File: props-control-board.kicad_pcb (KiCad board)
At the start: 2 copper layers, 109.2 x 35.6 mm, 64 parts, among them J1 Conn_01x04_Female, J10 Conn_01x02_Female, J11 Conn_01x02_Female, J12 Conn_01x02_Female, J13 Conn_01x02_Female, J2 Conn_01x03_Female, J3 Conn_01x03_Female, J4 Conn_01x03_Female, J5 Conn_01x06_Female, J6 Conn_01x05_Female, J7 Conn_01x04_Female, J8 Conn_01x02_Female, J9 Conn_01x02_Female, Q1 DMN24H3D5L, Q2 DMN24H3D5L, Q3 DMN24H3D5L, Q4 DMN24H3D5L, Q5 DMN24H3D5L, Q6 DMN24H3D5L, Q7 DMN24H3D5L, Q8 DMN24H3D5L, U1 AZ1117-3.3, U10 HCPL2631SD, U11 RFM-0505S, U2 VOS628A, U3 arduino_pro_mini, U4 STM32F042K6T6, U5 TXB0101DCKT, U6 TXB0104PWR, U7 AZ1117-3.3, U8 SX1278_module, U9 HCPL2631SD, Y1 Crystal_GND24

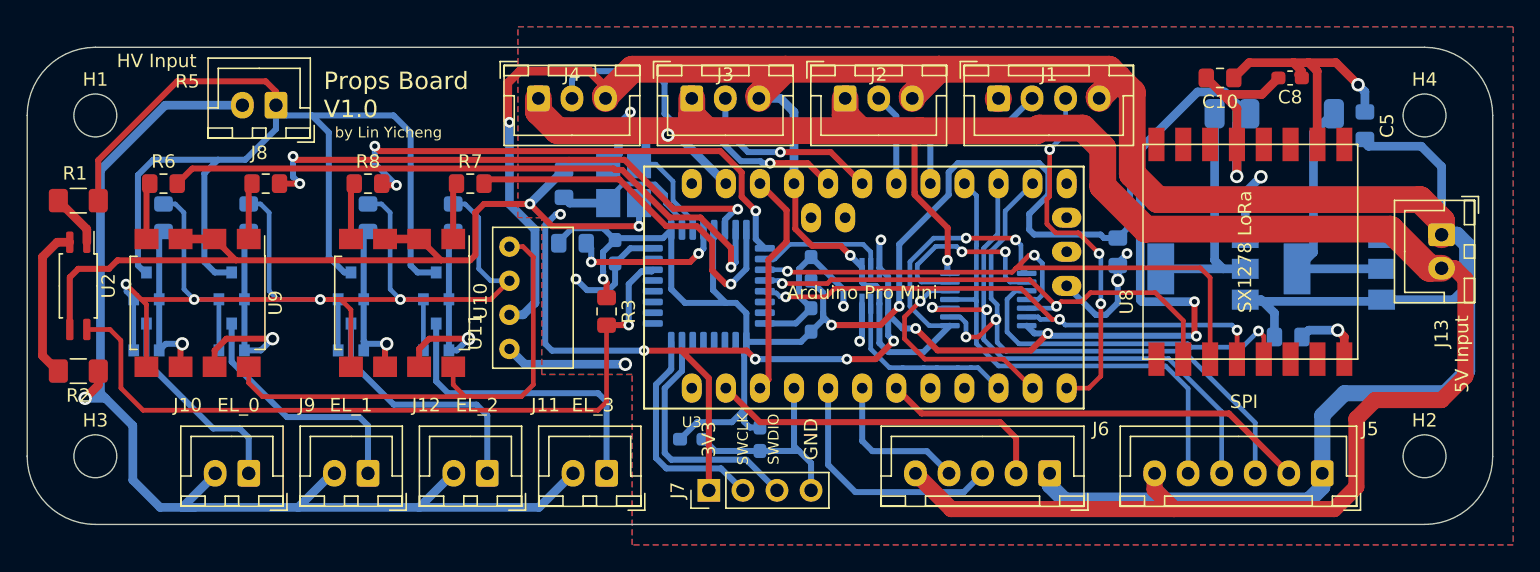
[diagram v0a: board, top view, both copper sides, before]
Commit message: expose more GPIO and expose UART
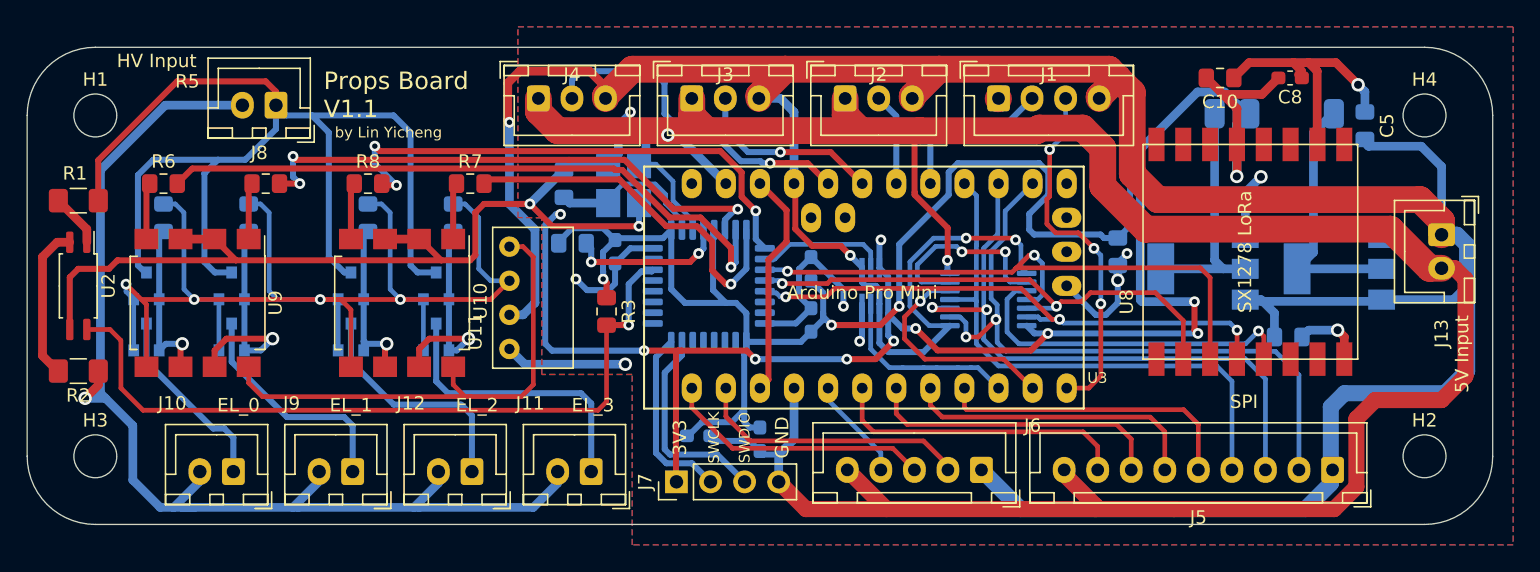
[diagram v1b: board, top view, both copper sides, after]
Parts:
- J5: value Conn_01x06_Female -> Conn_01x09_Female; footprint Connector_JST:JST_XH_B6B-XH-A_1x06_P2.50mm_Vertical -> Connector_JST:JST_XH_B9B-XH-A_1x09_P2.50mm_Vertical
- moved J6 5.09 mm to (160.0, 120.4)
- moved J7 2.50 mm to (137.3, 121.3)
- moved J10 1.15 mm to (104.3, 120.5)
- moved J11 1.15 mm to (130.9, 120.5)
- moved J12 1.15 mm to (122.0, 120.5)
- moved J9 1.15 mm to (113.2, 120.5)
- moved J5 0.80 mm to (186.2, 120.4)
- moved C7 0.57 mm to (138.9, 117.9)
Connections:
- net Net-(U3-Pad25) renamed /SDA
- net Net-(U3-Pad26) renamed /SCL
- net Net-(U3-Pad28) renamed /A6
- J5 pad 5: Net-(J5-Pad5) -> /D6
- J5 pad 6: GND -> /D5
- J6 pad 3: /D2 -> /TX
- J6 pad 4: /D3 -> /D2
- U3 pad 1: Net-(U3-Pad1) -> /TX
- U3 pad 14: Net-(J5-Pad3) -> Net-(J5-Pad2)
- U3 pad 15: Net-(J5-Pad4) -> Net-(J5-Pad3)
- U3 pad 16: Net-(J5-Pad5) -> Net-(J5-Pad4)
- U3 pad 7: Net-(J5-Pad2) -> /D4
- U3 pad 8: Net-(U3-Pad8) -> /D5
- U3 pad 9: Net-(U3-Pad9) -> /D6
- U6 pad 2: Net-(J5-Pad3) -> Net-(J5-Pad2)
- U6 pad 3: Net-(J5-Pad4) -> Net-(J5-Pad3)
- U6 pad 4: Net-(J5-Pad5) -> Net-(J5-Pad4)
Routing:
- net Net-(J5-Pad5): track 37.8 -> 0.00 mm
- net /D6: track 0.00 -> 22.8 mm
- net /D4: track 0.00 -> 22.5 mm
- net /D5: track 0.00 -> 22.4 mm
- net /TX: track 0.00 -> 20.0 mm
- net Net-(J5-Pad2): track 31.9 -> 49.5 mm, vias 0 -> 2
- net GND: track 329.6 -> 341.9 mm
- net /D3: track 11.4 -> 22.5 mm
- net /D2: track 18.6 -> 7.72 mm
- net 5V: track 245.8 -> 251.2 mm
- net /RX: track 25.8 -> 20.5 mm
- net /SWCLK: track 16.6 -> 13.7 mm
- net /SWDIO: track 18.3 -> 15.5 mm
- net Net-(J5-Pad3): track 44.4 -> 46.8 mm
- net 3V3: track 133.6 -> 132.1 mm
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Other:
- board text added: "Props Board V1.1"
- board text removed: "Props Board V1.0"

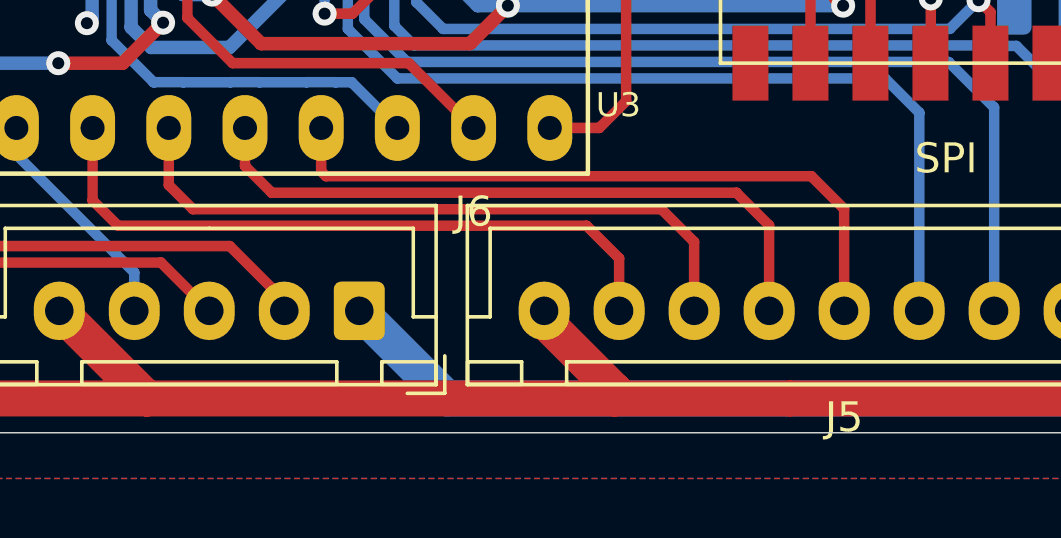
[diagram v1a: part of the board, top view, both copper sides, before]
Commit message: add reset connection to LoRa, add antenna connector
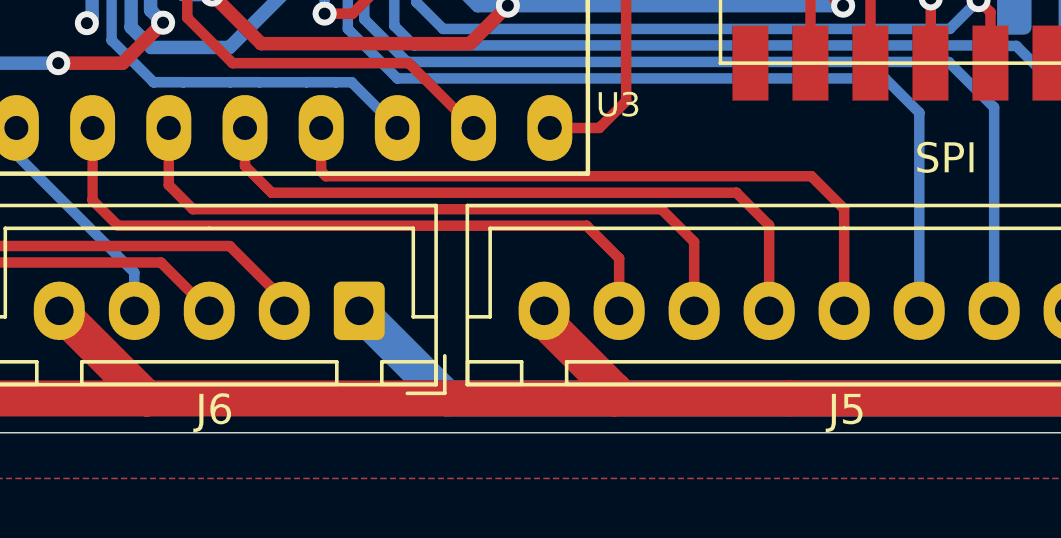
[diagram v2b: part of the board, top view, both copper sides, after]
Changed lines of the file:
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@@
     (descr "JST XH series connector, B9B-XH-A (http://www.jst-mfg.com/product/pdf/eng/eXH.pdf), generated with kicad-footprint-generator")
     (tags "connector JST XH vertical")
-    (fp_text reference J5 (at 10 -3.55) (layer F.SilkS)
+    (fp_text reference J5 (at 9.906 -3.302) (layer F.SilkS)
       (effects (font (size 1 1) (thickness 0.15)))
     )
@@
     (descr "JST XH series connector, B5B-XH-A (http://www.jst-mfg.com/product/pdf/eng/eXH.pdf), generated with kicad-footprint-generator")
     (tags "connector JST XH vertical")
-    (fp_text reference J6 (at -3.81 3.302) (layer F.SilkS)
-      (effects (font (size 1 1) (thickness 0.15)))
-    )
+    (fp_text reference J6 (at 4.826 -3.302) (layer F.SilkS)
+      (effects (font (size 1 1) (thickness 0.15)))
+    )
